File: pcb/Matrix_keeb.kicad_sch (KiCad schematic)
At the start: 81 parts, among them K1 KEYSW, K10 KEYSW, K11 KEYSW, K12 KEYSW, K13 KEYSW, K14 KEYSW, K15 KEYSW, K16 KEYSW, K17 KEYSW, K18 KEYSW, K19 KEYSW, K2 KEYSW, K20 KEYSW, K21 KEYSW, K22 KEYSW, K23 KEYSW, K24 KEYSW, K25 KEYSW, K26 KEYSW, K27 KEYSW, K28 KEYSW, K29 KEYSW, K3 KEYSW, K30 KEYSW, K31 KEYSW, K32 KEYSW, K33 KEYSW, K34 KEYSW, K35 KEYSW, K36 KEYSW, K37 KEYSW, K38 KEYSW, K39 KEYSW, K4 KEYSW, K40 KEYSW, K41 KEYSW, K42 KEYSW, K43 KEYSW, K44 KEYSW, K45 KEYSW, K46 KEYSW, K47 KEYSW, K48 KEYSW, K49 KEYSW, K5 KEYSW, K50 KEYSW, K51 KEYSW, K52 KEYSW, K6 KEYSW, K7 KEYSW, K8 KEYSW, K9 KEYSW, SW1 RotaryEncoder_Switch, SW3 RotaryEncoder_Switch

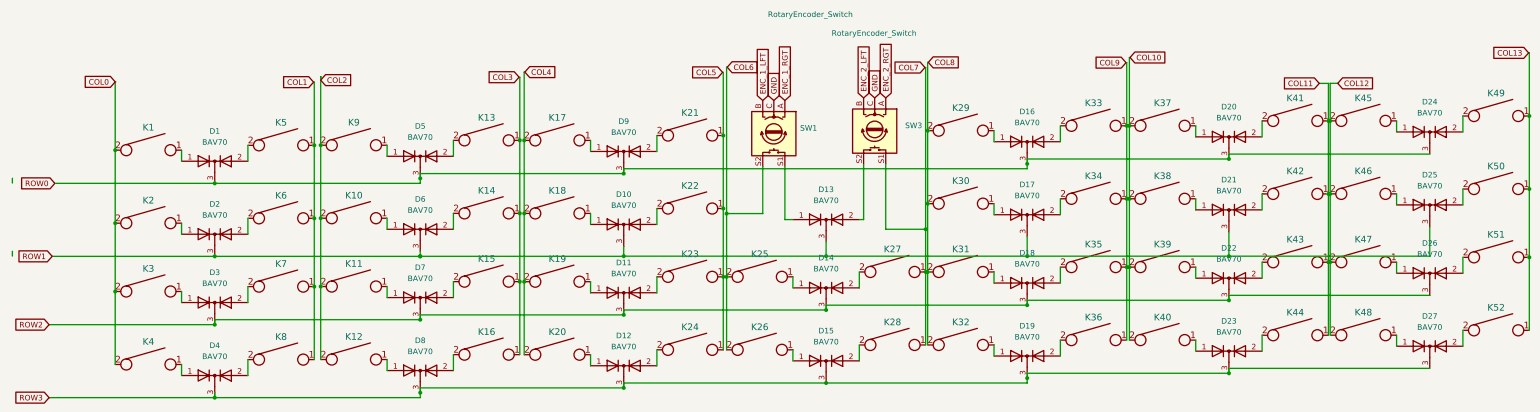
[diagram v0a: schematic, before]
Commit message: updated pcb
added onboard mcu
included silkscreen resembling sun and SOHO
added files for assembly with jlcpcb
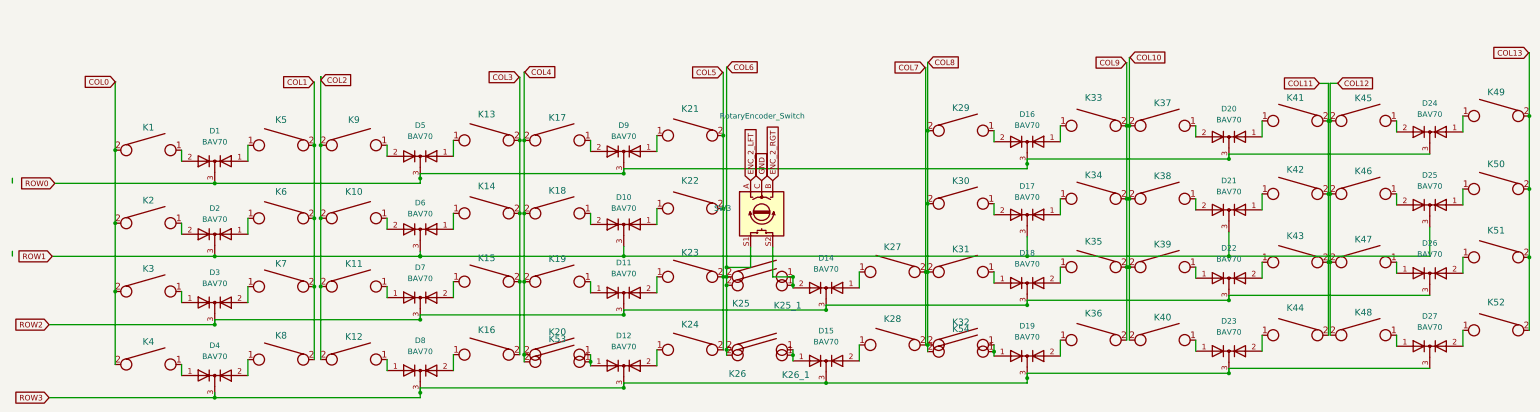
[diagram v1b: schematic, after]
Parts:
- removed D13: BAV70, Package_TO_SOT_SMD:SOT-23, symbol Diode:BAV70
- removed SW1: RotaryEncoder_Switch, Keebio-Parts:RotaryEncoder_Alps_EC11E-Switch_Vertical_H20mm, symbol Device:RotaryEncoder_Switch
- added K25_1, K26_1, K53, K54: KEYSW, keyswitches:Kailh_socket_PG1350_optional, symbol keyboard_parts:KEYSW
- D1, D10, D11, D12, D14, D15, D16, D17, D18, D19, D2, D20, D21, D22, D23, D24, D25, D26, D27, D3, D4, D5, D6, D7, D8, D9: LCSC (none) -> C68978
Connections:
- net COL1: now also K5.2, K6.2, K7.2, K8.2; no longer K5.1, K6.1, K7.1, K8.1
- net COL11: now also K41.2, K42.2, K43.2, K44.2; no longer K41.1, K42.1, K43.1, K44.1
- net COL13: now also K49.2, K50.2, K51.2, K52.2; no longer K49.1, K50.1, K51.1, K52.1
- net COL3: now also K13.2, K14.2, K15.2, K16.2; no longer K13.1, K14.1, K15.1, K16.1
- net COL4: now also K53.2
- net COL5: now also K21.2, K22.2, K23.2, K24.2; no longer K21.1, K22.1, K23.1, K24.1
- net COL6: now also SW3.S1, K25_1.2, K26_1.2
- net COL7: now also K27.2, K28.2; no longer K27.1, K28.1, SW3.S1
- net COL8: now also K54.2
- net COL9: now also K33.2, K34.2, K35.2, K36.2; no longer K33.1, K34.1, K35.1, K36.1
- net ENC_2_LFT: now also SW3.A; no longer SW3.B
- net ENC_2_RGT: now also SW3.B; no longer SW3.A
- net at SW3.S2: now also D14.2 (A), K25.1, K25_1.1
- net at K38.1: now also D21.2 (A); no longer D21.1 (A)
- net at D27.2 (A): now also K52.1; no longer K52.2
- net at D12.1 (A), K20.1: now also K53.1
- net at D12.2 (A): now also K24.1; no longer K24.2
- net at K18.1: now also D10.2 (A); no longer D10.1 (A)
- net at D24.2 (A): now also K45.1; no longer K49.2
- net at D7.2 (A): now also K15.1; no longer K15.2
- net at K37.1: now also D20.2 (A); no longer D20.1 (A)
- net at D14.1 (A): now also K27.1; no longer K25.1
- net at D8.2 (A): now also K16.1; no longer K16.2
- net at K9.1: now also D5.2 (A); no longer D5.1 (A)
- net at K2.1: now also D2.2 (A); no longer D2.1 (A)
- net at D16.1 (A): now also K33.1; no longer K29.1
- net at D16.2 (A): now also K29.1; no longer K33.2
- net at D19.2 (A): now also K36.1; no longer K36.2
- net at D15.1 (A), K26.1: now also K26_1.1
- net at D6.1 (A): now also K14.1; no longer K10.1
- net at D6.2 (A): now also K10.1; no longer K14.2
- net at D25.2 (A): now also K46.1; no longer K50.2
- net at D22.2 (A): now also K43.1; no longer K43.2
- net at K1.1: now also D1.2 (A); no longer D1.1 (A)
- net at D24.1 (A): now also K49.1; no longer K45.1
- net at D26.2 (A): now also K51.1; no longer K51.2
- net at D11.2 (A): now also K23.1; no longer K23.2
- net at D9.2 (A): now also K17.1; no longer K21.2
- net at D25.1 (A): now also K50.1; no longer K46.1
- net at D18.2 (A): now also K35.1; no longer K35.2
- net at D15.2 (A): now also K28.1; no longer K28.2
- net at D19.1 (A), K32.1: now also K54.1
- net at D3.2 (A): now also K7.1; no longer K7.2
- net at D23.2 (A): now also K44.1; no longer K44.2
- net at D9.1 (A): now also K21.1; no longer K17.1
- net at D4.2 (A): now also K8.1; no longer K8.2
- net at K30.1: now also D17.2 (A); no longer D17.1 (A)
- new net: D10.1 (A), K22.1
- new net: D2.1 (A), K6.1
- new net: D20.1 (A), K41.1
- new net: D1.1 (A), K5.1
- new net: D21.1 (A), K42.1
- new net: D5.1 (A), K13.1
- new net: D17.1 (A), K34.1
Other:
- moved on the sheet: SW3
